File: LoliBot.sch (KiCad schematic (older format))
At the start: 37 parts, among them J1 LOLINBATT, J10 LEFT-MOTOR, J11 REFLECT_, J12 MECH, J13 MECH, J14 MECH, J15 MECH, J16 MECH, J17 MECH, J18 MECH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

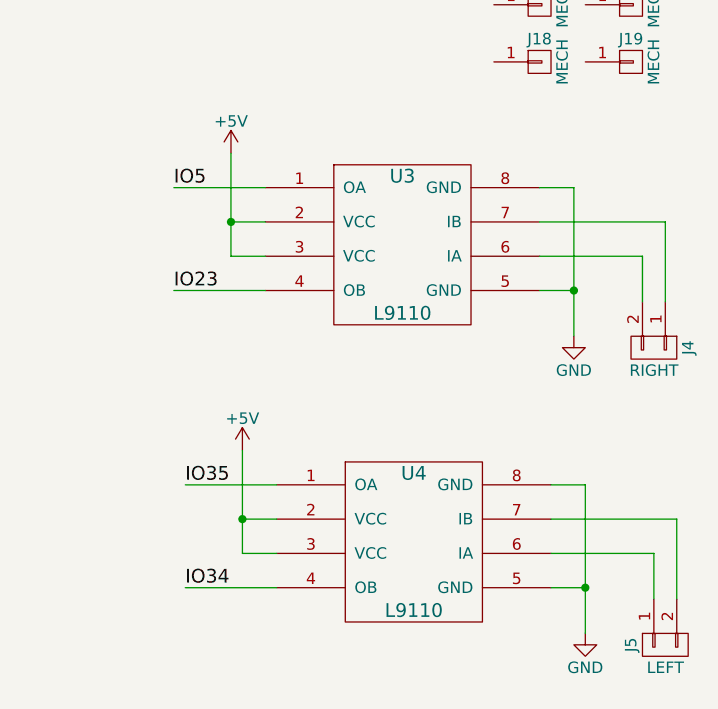
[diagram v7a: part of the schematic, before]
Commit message: Whoops, those L9110 Pins don't go there.
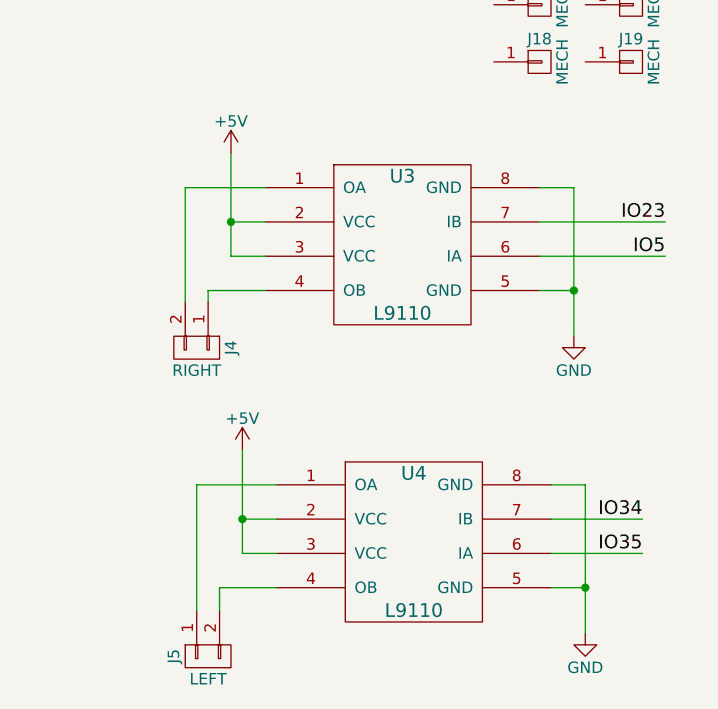
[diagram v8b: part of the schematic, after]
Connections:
- net IO23: now also U3.7 (IB); no longer U3.4 (OB)
- net IO34: now also U4.7 (IB); no longer U4.4 (OB)
- net IO35: now also U4.6 (IA); no longer U4.1 (OA)
- net IO5: now also U3.6 (IA); no longer U3.1 (OA)
- net at J4.2 (P2): now also U3.1 (OA); no longer U3.6 (IA)
- net at J4.1 (P1): now also U3.4 (OB); no longer U3.7 (IB)
- net at J5.1 (P1): now also U4.1 (OA); no longer U4.6 (IA)
- net at J5.2 (P2): now also U4.4 (OB); no longer U4.7 (IB)
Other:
- moved on the sheet: J4, J5
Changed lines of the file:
@@
 L CONN_01X02 J4
 U 1 1 59DBB5AA
-P 10800 4800
-F 0 "J4" H 10800 4950 50  0000 C CNN
-F 1 "RIGHT" V 10900 4800 50  0000 C CNN
-F 2 "Pin_Headers:Pin_Header_Straight_1x02_Pitch2.00mm" H 10800 4800 50  0001 C CNN
-F 3 "" H 10800 4800 50  0001 C CNN
-	1    10800 4800
+P 8800 4800
+F 0 "J4" H 8800 4950 50  0000 C CNN
+F 1 "RIGHT" V 8900 4800 50  0000 C CNN
+F 2 "Pin_Headers:Pin_Header_Straight_1x02_Pitch2.00mm" H 8800 4800 50  0001 C CNN
+F 3 "" H 8800 4800 50  0001 C CNN
+	1    8800 4800
 	0    1    1    0
 $EndComp
@@
 Connection ~ 10450 4550
 Wire Wire Line
-	10300 4400 10750 4400
-Wire Wire Line
-	10750 4400 10750 4600
+	10300 4400 10850 4400
 Wire Wire Line
 	10300 4250 10850 4250
-Wire Wire Line
-	10850 4250 10850 4600
 $Comp
 L +5V #PWR013
@@
 	9100 4250 8950 4250
 Connection ~ 8950 4250
-Wire Wire Line
-	9100 4100 8700 4100
-Wire Wire Line
-	9100 4550 8700 4550
-Text Label 8700 4100 0    60   ~ 0
+Text Label 10850 4400 2    60   ~ 0
 IO5
-Text Label 8700 4550 0    60   ~ 0
+Text Label 10850 4250 2    60   ~ 0
 IO23
 $Comp
@@
 L CONN_01X02 J5
 U 1 1 59DBCDBD
-P 10850 6100
-F 0 "J5" H 10850 6250 50  0000 C CNN
-F 1 "LEFT" V 10950 6100 50  0000 C CNN
-F 2 "Pin_Headers:Pin_Header_Straight_1x02_Pitch2.00mm" H 10850 6100 50  0001 C CNN
-F 3 "" H 10850 6100 50  0001 C CNN
-	1    10850 6100
+P 8850 6150
+F 0 "J5" H 8850 6300 50  0000 C CNN
+F 1 "LEFT" V 8950 6150 50  0000 C CNN
+F 2 "Pin_Headers:Pin_Header_Straight_1x02_Pitch2.00mm" H 8850 6150 50  0001 C CNN
+F 3 "" H 8850 6150 50  0001 C CNN
+	1    8850 6150
 	0    -1   1    0
 $EndComp
@@
 Connection ~ 10500 5850
 Wire Wire Line
-	10350 5700 10800 5700
-Wire Wire Line
-	10800 5700 10800 5900
-Wire Wire Line
-	10350 5550 10900 5550
-Wire Wire Line
-	10900 5550 10900 5900
+	10350 5700 10750 5700
+Wire Wire Line
+	10350 5550 10750 5550
 $Comp
 L +5V #PWR015
@@
 	9150 5550 9000 5550
 Connection ~ 9000 5550
-Wire Wire Line
-	9150 5400 8750 5400
-Wire Wire Line
-	9150 5850 8750 5850
-Text Label 8750 5850 0    60   ~ 0
+Text Label 10750 5550 2    60   ~ 0
 IO34
-Text Label 8750 5400 0    60   ~ 0
+Text Label 10750 5700 2    60   ~ 0
 IO35
 $Comp
@@
 	1    0    0    -1
 $EndComp
+Wire Wire Line
+	8850 4600 8850 4550
+Wire Wire Line
+	8850 4550 9100 4550
+Wire Wire Line
+	9100 4100 8750 4100
+Wire Wire Line
+	8750 4100 8750 4600
+Wire Wire Line
+	9150 5850 8900 5850
+Wire Wire Line
+	8900 5850 8900 5950
+Wire Wire Line
+	9150 5400 8800 5400
+Wire Wire Line
+	8800 5400 8800 5950
 $EndSCHEMATC
